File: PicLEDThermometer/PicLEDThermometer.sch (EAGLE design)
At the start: 17 parts, among them IC1 74LS595N, Q1 MCP1702-3302E/TO

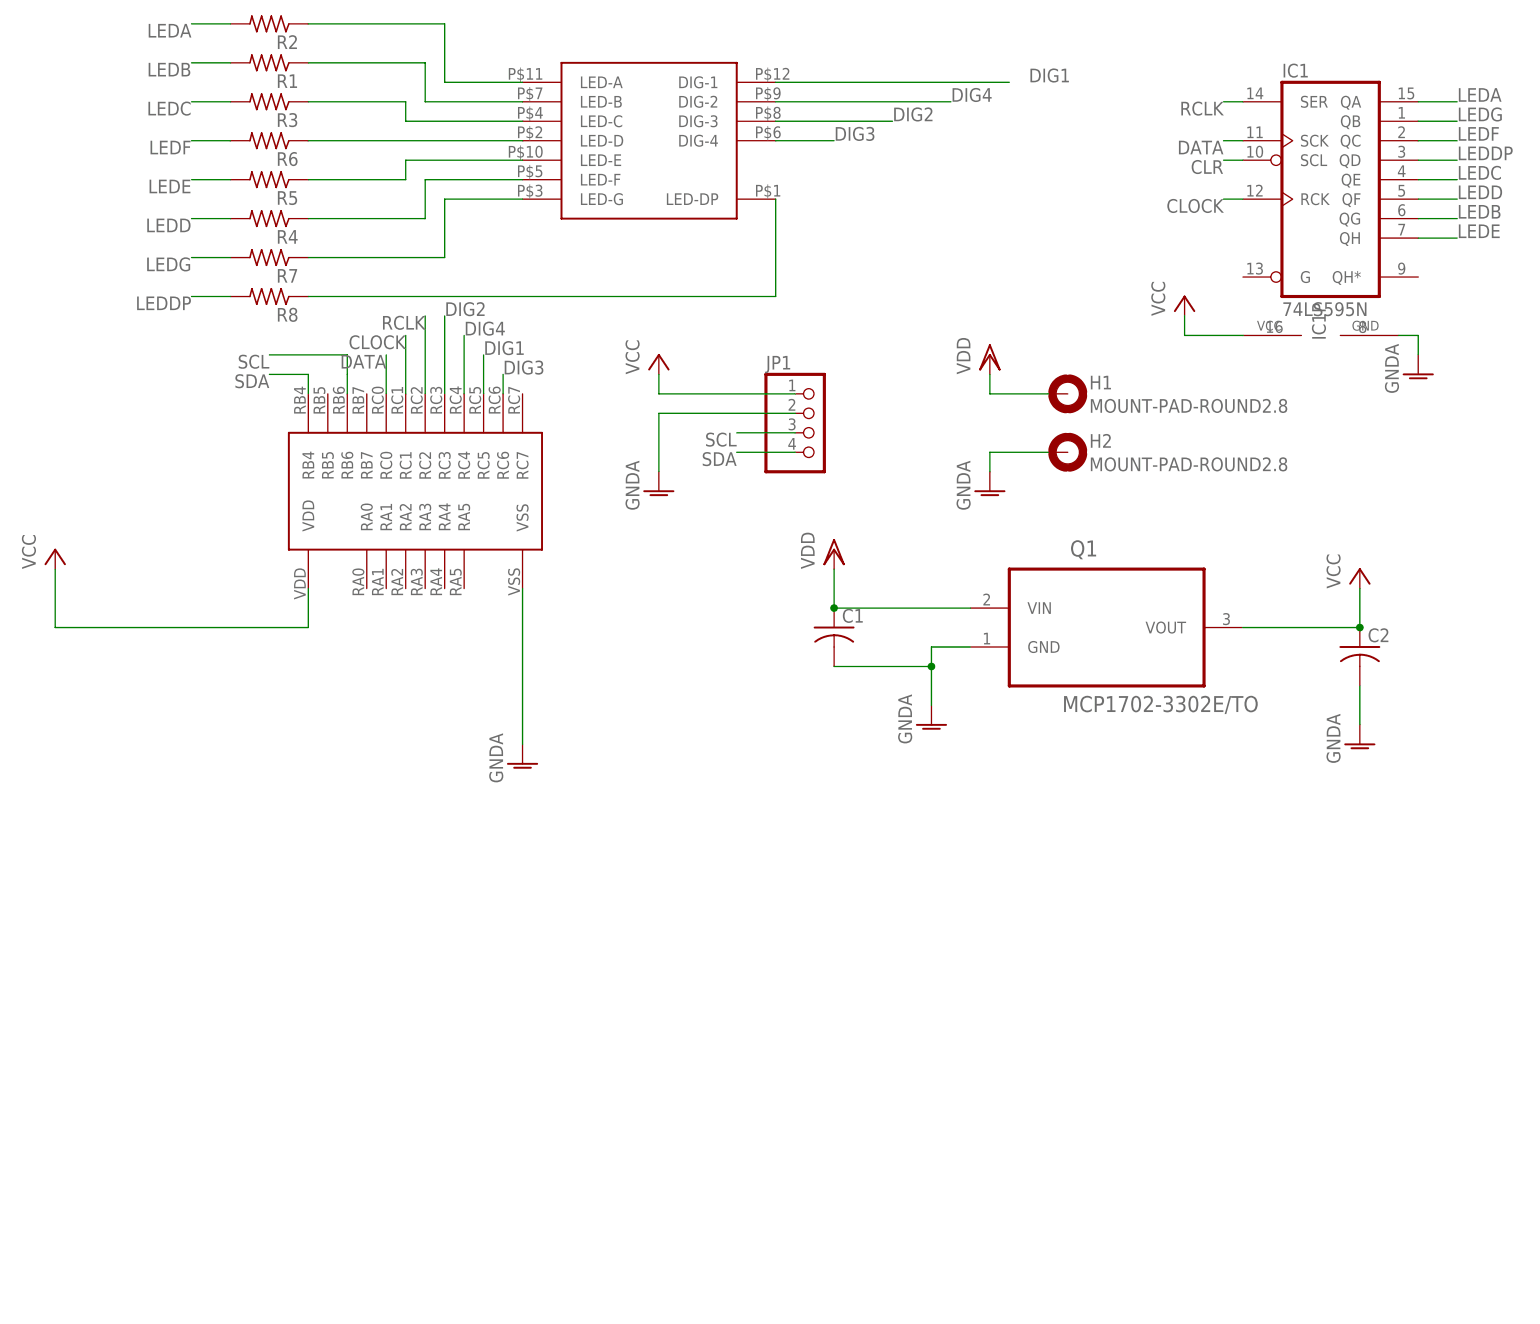
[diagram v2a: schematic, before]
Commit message: Add a programming header. Moved I2C connector. Changed power connector to 2 pin header. Updated label to v0.2.
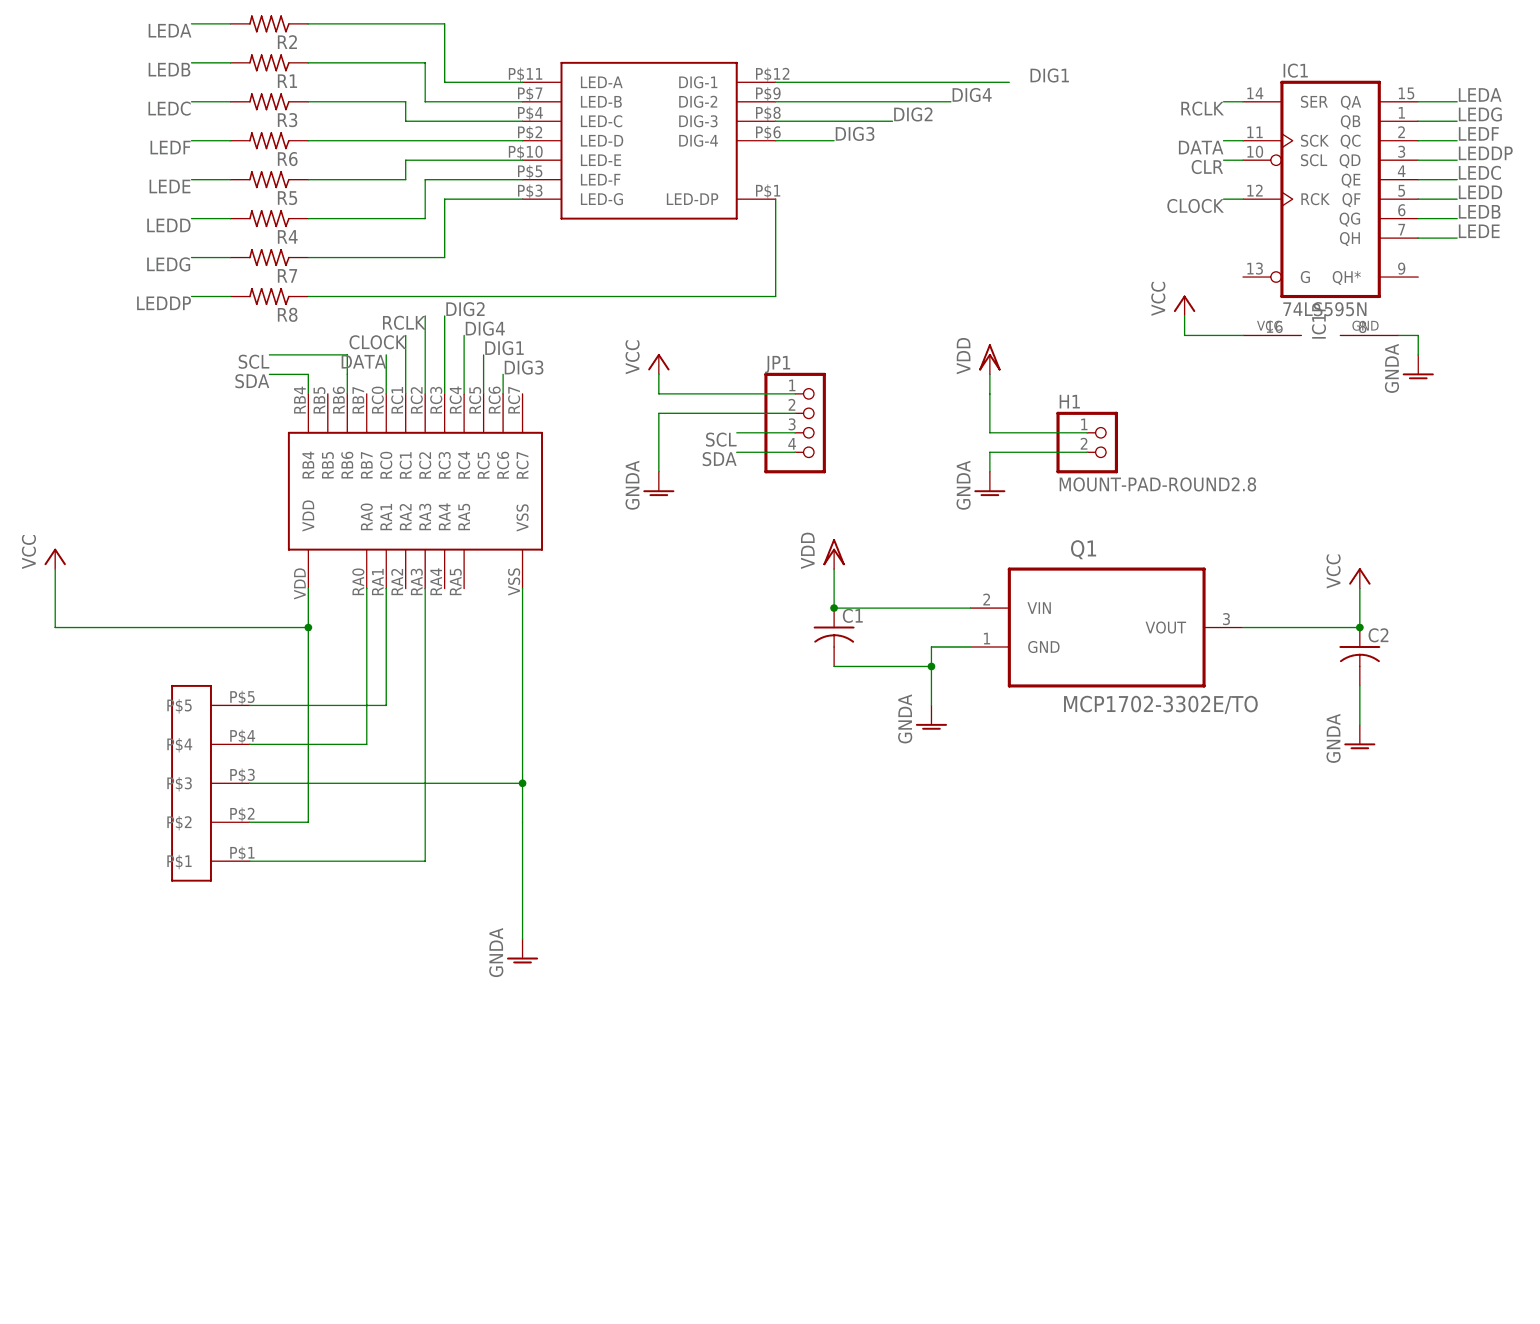
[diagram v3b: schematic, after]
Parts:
- removed H2: MOUNT-PAD-ROUND2.8, holes:MOUNT-PAD-ROUND2.8
- added U$3: JST-PH-5POS, con-JST:JST-PH-5POS
- H1: device holes:MOUNT-PAD-ROUND2.8 -> pinhead:PINHD-1X2
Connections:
- new net N$10: U$2.RA1, U$3.P$5
- new net N$8: U$2.RA3, U$3.P$1
- new net N$9: U$2.RA0, U$3.P$4
- net GNDA: now also H1.2, U$3.P$3; no longer H2.MOUNT
- net VCC: now also U$3.P$2
- net VDD: now also H1.1; no longer H1.MOUNT
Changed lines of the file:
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@@
 <?xml version="1.0" encoding="utf-8"?>
 <!DOCTYPE eagle SYSTEM "eagle.dtd">
-<eagle version="8.2.2">
+<eagle version="9.1.0">
 <drawing>
 <settings>
 <setting alwaysvectorfont="no"/>
+<setting keepoldvectorfont="yes"/>
 <setting verticaltext="up"/>
 </settings>
@@
 <part name="C2" library="rcl" library_urn="urn:adsk.eagle:library:334" deviceset="C-US" device="025-030X050"/>
 <part name="GND6" library="supply1" library_urn="urn:adsk.eagle:library:371" deviceset="GNDA" device=""/>
-<part name="H1" library="holes" library_urn="urn:adsk.eagle:library:237" deviceset="MOUNT-PAD-ROUND" device="2.8" value="MOUNT-PAD-ROUND2.8"/>
-<part name="H2" library="holes" library_urn="urn:adsk.eagle:library:237" deviceset="MOUNT-PAD-ROUND" device="2.8" value="MOUNT-PAD-ROUND2.8"/>
+<part name="H1" library="pinhead" library_urn="urn:adsk.eagle:library:325" deviceset="PINHD-1X2" device="" package3d_urn="urn:adsk.eagle:package:22435/2" value="MOUNT-PAD-ROUND2.8"/>
 <part name="VDD3" library="supply1" deviceset="VDD" device=""/>
 <part name="GND7" library="supply1" library_urn="urn:adsk.eagle:library:371" deviceset="GNDA" device=""/>
+<part name="U$3" library="con-JST" deviceset="JST-PH-5POS" device=""/>
 </parts>
 <sheets>
@@
 <instance part="R7" gate="G$1" x="20.32" y="55.88" rot="R180"/>
 <instance part="U$2" gate="G$1" x="40.64" y="20.32" rot="R90"/>
-<instance part="GND2" gate="1" x="53.34" y="-10.16"/>
+<instance part="GND2" gate="1" x="53.34" y="-35.56"/>
 <instance part="R8" gate="G$1" x="20.32" y="50.8" rot="R180"/>
 <instance part="IC1" gate="A" x="157.48" y="66.04"/>
@@
 <instance part="C2" gate="G$1" x="162.56" y="5.08"/>
 <instance part="GND6" gate="1" x="162.56" y="-7.62"/>
-<instance part="H1" gate="G$1" x="124.46" y="38.1"/>
-<instance part="H2" gate="G$1" x="124.46" y="30.48"/>
+<instance part="H1" gate="G$1" x="129.54" y="30.48"/>
 <instance part="VDD3" gate="G$1" x="114.3" y="43.18"/>
 <instance part="GND7" gate="1" x="114.3" y="25.4"/>
+<instance part="U$3" gate="G$1" x="10.16" y="-20.32" rot="R180"/>
 </instances>
 <busses>
@@
 <pinref part="U$2" gate="G$1" pin="VSS"/>
 <pinref part="GND2" gate="1" pin="GNDA"/>
-<wire x1="53.34" y1="12.7" x2="53.34" y2="-7.62" width="0.1524" layer="91"/>
+<wire x1="53.34" y1="12.7" x2="53.34" y2="-12.7" width="0.1524" layer="91"/>
+<wire x1="53.34" y1="-12.7" x2="53.34" y2="-17.78" width="0.1524" layer="91"/>
+<wire x1="53.34" y1="-17.78" x2="53.34" y2="-33.02" width="0.1524" layer="91"/>
+<pinref part="U$3" gate="G$1" pin="P$3"/>
+<wire x1="17.78" y1="-12.7" x2="53.34" y2="-12.7" width="0.1524" layer="91"/>
+<junction x="53.34" y="-12.7"/>
 </segment>
 <segment>
@@
 <pinref part="GND7" gate="1" pin="GNDA"/>
 <wire x1="114.3" y1="30.48" x2="114.3" y2="27.94" width="0.1524" layer="91"/>
-<pinref part="H2" gate="G$1" pin="MOUNT"/>
-<wire x1="114.3" y1="30.48" x2="121.92" y2="30.48" width="0.1524" layer="91"/>
+<wire x1="114.3" y1="30.48" x2="127" y2="30.48" width="0.1524" layer="91"/>
+<pinref part="H1" gate="G$1" pin="2"/>
 </segment>
 </net>
@@
 <wire x1="7.62" y1="7.62" x2="-7.62" y2="7.62" width="0.1524" layer="91"/>
 <wire x1="-7.62" y1="7.62" x2="-7.62" y2="15.24" width="0.1524" layer="91"/>
+<pinref part="U$3" gate="G$1" pin="P$2"/>
+<wire x1="17.78" y1="-17.78" x2="25.4" y2="-17.78" width="0.1524" layer="91"/>
+<wire x1="25.4" y1="-17.78" x2="25.4" y2="7.62" width="0.1524" layer="91"/>
+<junction x="25.4" y="7.62"/>
 </segment>
 <segment>
@@
 <pinref part="VDD3" gate="G$1" pin="VDD"/>
 <wire x1="114.3" y1="38.1" x2="114.3" y2="40.64" width="0.1524" layer="91"/>
-<pinref part="H1" gate="G$1" pin="MOUNT"/>
-<wire x1="114.3" y1="38.1" x2="121.92" y2="38.1" width="0.1524" layer="91"/>
+<pinref part="H1" gate="G$1" pin="1"/>
+<wire x1="127" y1="33.02" x2="114.3" y2="33.02" width="0.1524" layer="91"/>
+<wire x1="114.3" y1="33.02" x2="114.3" y2="38.1" width="0.1524" layer="91"/>
+</segment>
+</net>
+<net name="N$8" class="0">
+<segment>
+<pinref part="U$2" gate="G$1" pin="RA3"/>
+<wire x1="40.64" y1="12.7" x2="40.64" y2="-22.86" width="0.1524" layer="91"/>
+<pinref part="U$3" gate="G$1" pin="P$1"/>
+<wire x1="40.64" y1="-22.86" x2="17.78" y2="-22.86" width="0.1524" layer="91"/>
+</segment>
+</net>
+<net name="N$9" class="0">
+<segment>
+<pinref part="U$2" gate="G$1" pin="RA0"/>
+<pinref part="U$3" gate="G$1" pin="P$4"/>
+<wire x1="33.02" y1="12.7" x2="33.02" y2="-7.62" width="0.1524" layer="91"/>
+<wire x1="33.02" y1="-7.62" x2="17.78" y2="-7.62" width="0.1524" layer="91"/>
+</segment>
+</net>
+<net name="N$10" class="0">
+<segment>
+<pinref part="U$2" gate="G$1" pin="RA1"/>
+<pinref part="U$3" gate="G$1" pin="P$5"/>
+<wire x1="35.56" y1="12.7" x2="35.56" y2="-2.54" width="0.1524" layer="91"/>
+<wire x1="35.56" y1="-2.54" x2="17.78" y2="-2.54" width="0.1524" layer="91"/>
 </segment>
 </net>
@@
 <compatibility>
 <note version="8.2" severity="warning">
-Since Version 8.2, Eagle supports online libraries. The ids
+Since Version 8.2, EAGLE supports online libraries. The ids
 of those online libraries will not be understood (or retained)
 with this version.
 </note>
+<note version="8.3" severity="warning">
+Since Version 8.3, EAGLE supports URNs for individual library
+assets (packages, symbols, and devices). The URNs of those assets
+will not be understood (or retained) with this version.
+</note>
+<note version="8.3" severity="warning">
+Since Version 8.3, EAGLE supports the association of 3D packages
+with devices in libraries, schematics, and board files. Those 3D
+packages will not be understood (or retained) with this version.
+</note>
 </compatibility>

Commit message: Add NPN transistors for LED cathodes. Add pull ups for I2C lines.
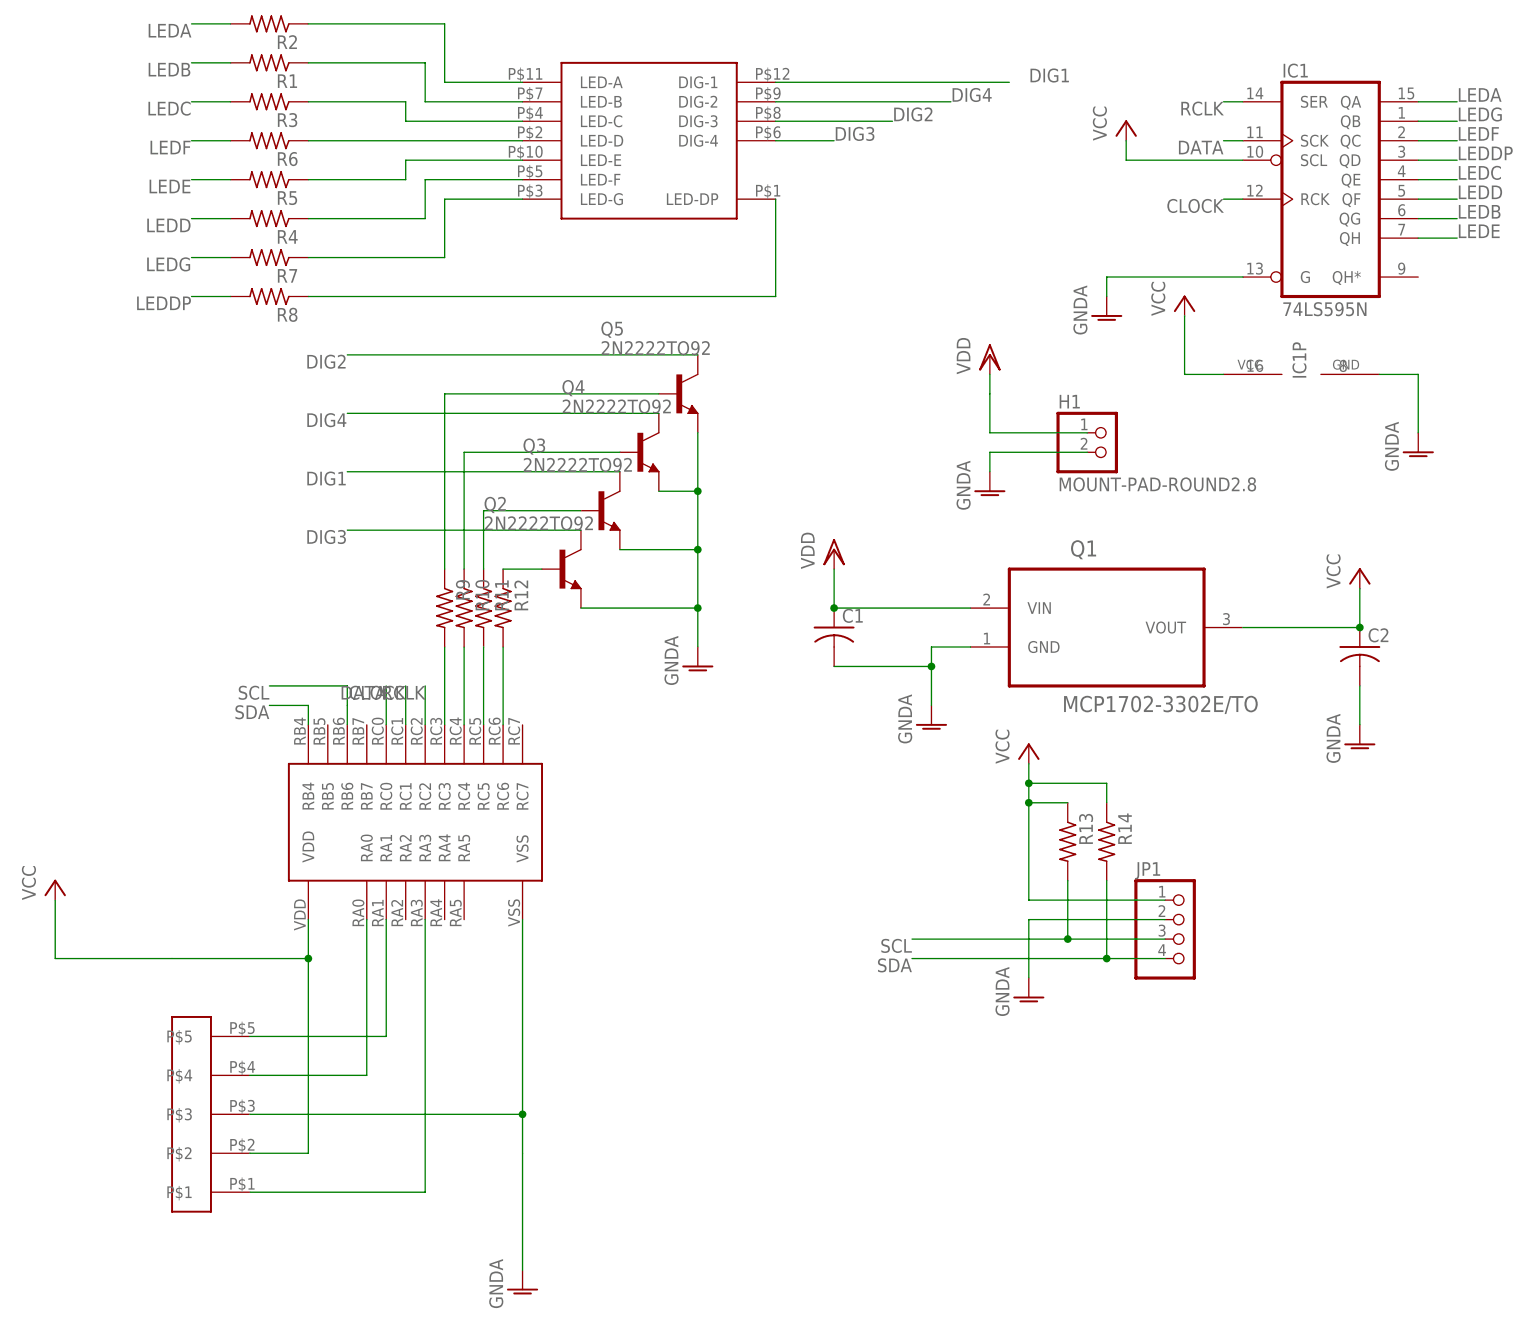
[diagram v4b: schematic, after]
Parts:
- added Q2, Q3, Q4, Q5: 2N2222TO92, 2n2222:2N2222TO92
- added R10, R11, R12, R13, R14, R9: (no value), rcl:R-US_0207/10
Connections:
- removed net CLR: IC1A.SCL
- new net N$11: R12.2, U$2.RC6
- new net N$13: R11.2, U$2.RC5
- new net N$14: R10.2, U$2.RC4
- new net N$15: R9.2, U$2.RC3
- new net N$16: Q2.B, R12.1
- new net N$17: Q3.B, R11.1
- new net N$18: Q4.B, R10.1
- new net N$19: Q5.B, R9.1
- net DIG1: now also Q3.C; no longer U$2.RC5
- net DIG2: now also Q5.C; no longer U$2.RC3
- net DIG3: now also Q2.C; no longer U$2.RC6
- net DIG4: now also Q4.C; no longer U$2.RC4
- net GNDA: now also IC1A.G, Q2.E, Q3.E, Q4.E, Q5.E
- net SCL: now also R13.2
- net SDA: now also R14.2
- net VCC: now also IC1A.SCL, R13.1, R14.1
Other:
- moved on the sheet: IC1P, JP1
